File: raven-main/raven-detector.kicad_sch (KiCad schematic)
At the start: 5 parts, among them U4 OPA656UB, U5 TLV3201AIDCKT

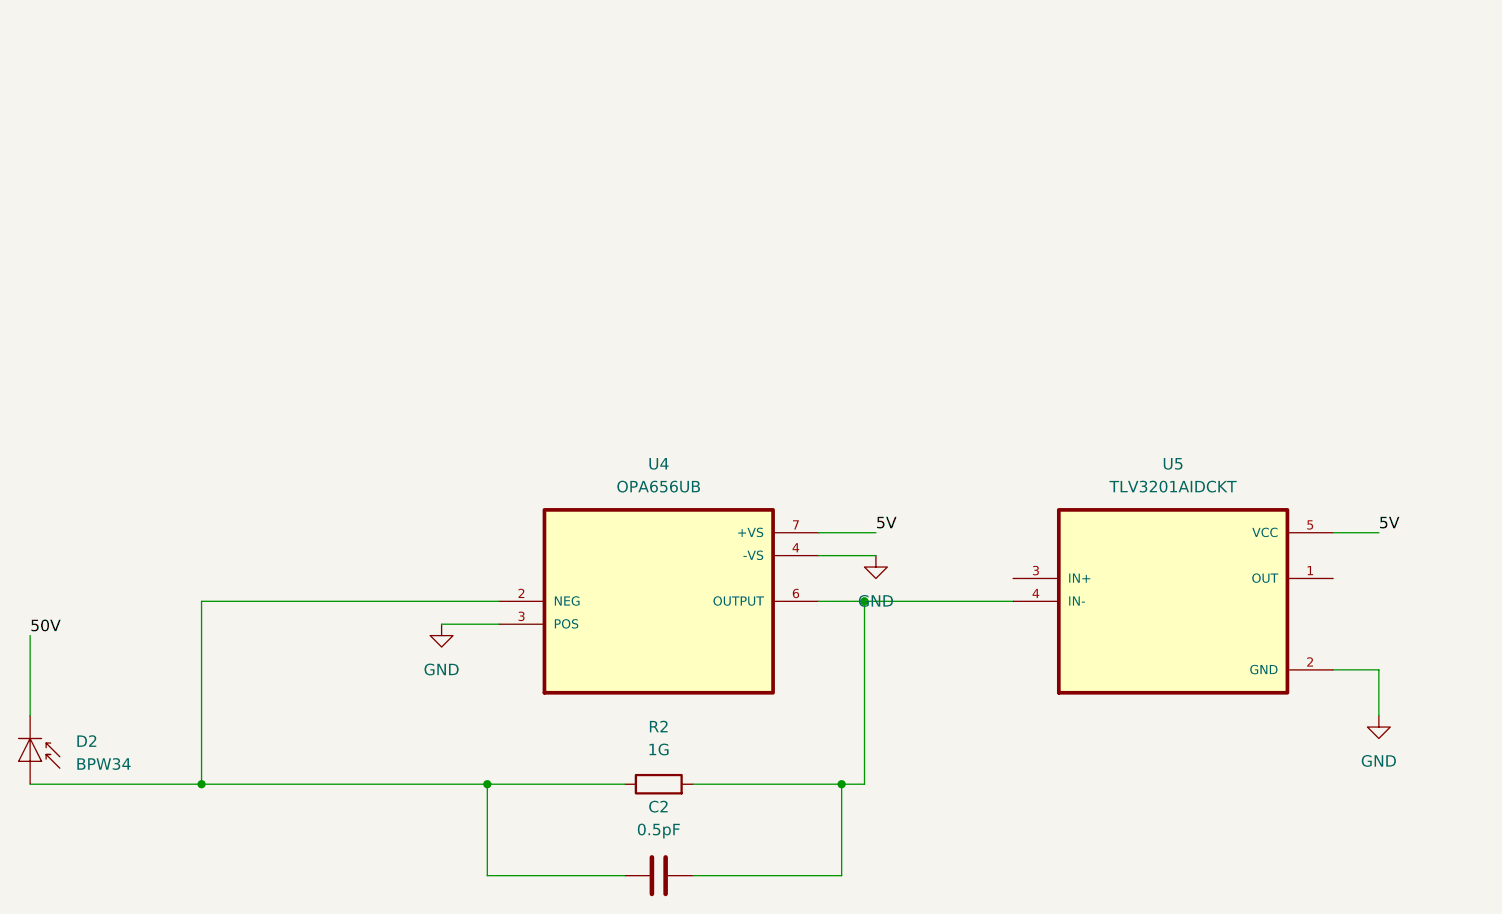
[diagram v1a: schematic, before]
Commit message: Added LDO Regulator
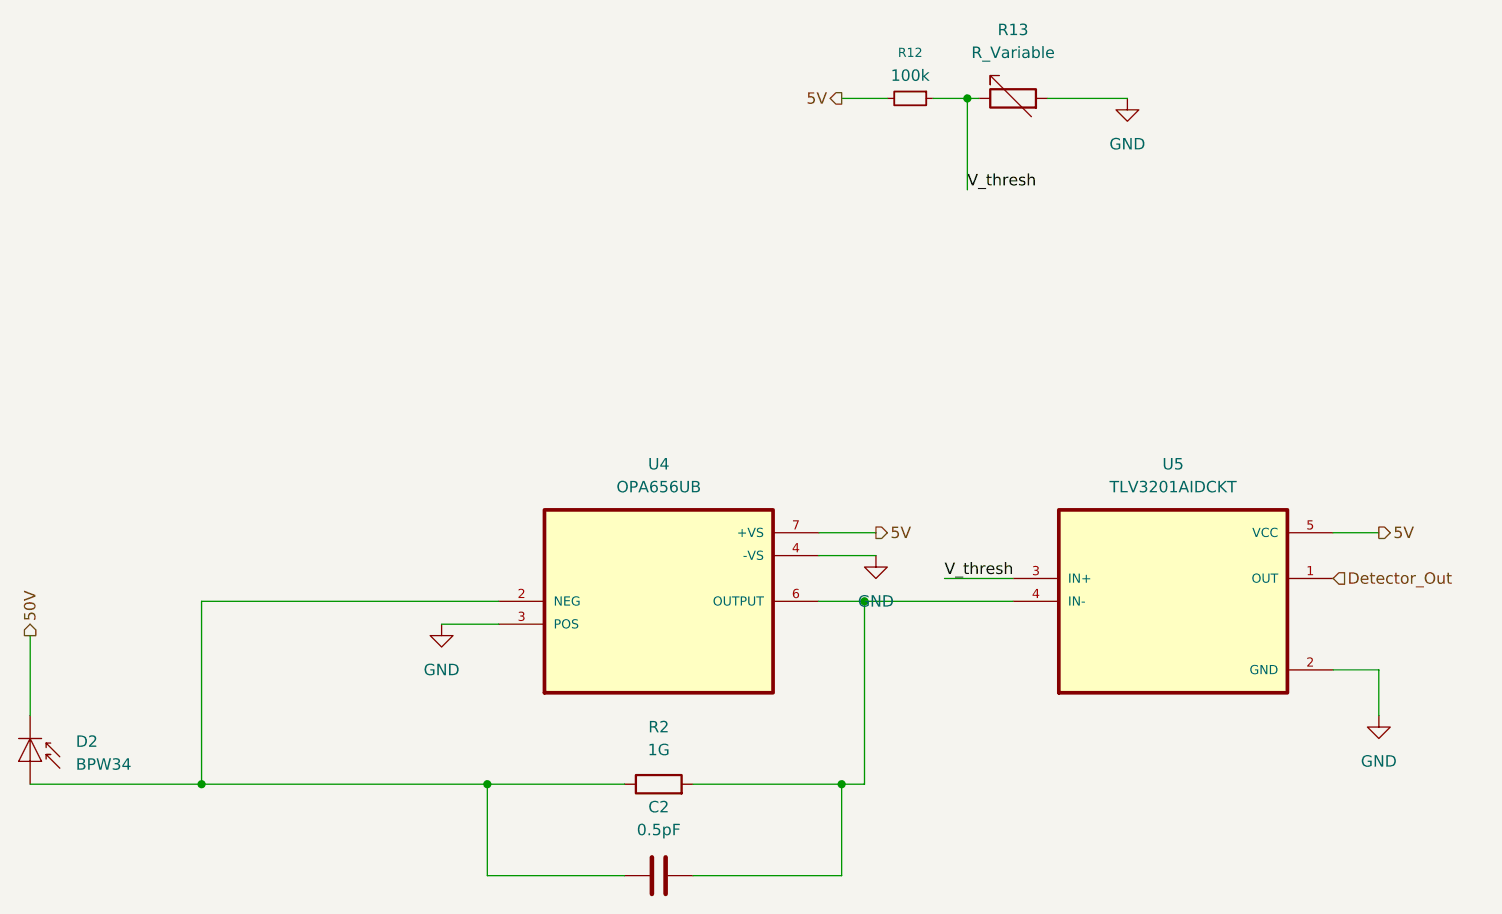
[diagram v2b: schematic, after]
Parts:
- added R12: 100k, symbol Device:R_Small
- added R13: R_Variable, symbol Device:R_Variable
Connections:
- net 5V: now also R12.2
- net GND: now also R13.2
- net Detector_Out: now reaches U5.1 (OUT)
- net V_thresh: now reaches U5.3 (IN+)
- net V_thresh: now also R12.1, R13.1
